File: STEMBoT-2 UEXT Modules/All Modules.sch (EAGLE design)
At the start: 132 parts, among them IC1 74HC165PW,118, IC2 74HC165PW,118, IC3 74HC165PW,118, J1 FTSH-105-01-XXX-DV-K, J2 FTSH-105-01-XXX-DV-K, J3 FTSH-105-01-XXX-DV-K, J4 FTSH-105-01-XXX-DV-K, J5 FTSH-105-01-XXX-DV-K, J6 FTSH-105-01-XXX-DV-K, Q1 MMBT3904LP-7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

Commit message: final pcb board layout for reveiw
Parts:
- added R56, R59, R60: ERJ-1RHD3601C, Resistor:ERJ-1RHD3601C
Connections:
- removed net N$145: IC2.!PL, U$2.MOSI
- removed net N$159: R61.1
- removed net N$163: IC3.!PL, U$1.MOSI
- removed net N$2: U1.OUT
- new net N$158: IC3.!PL, R56.1, U$1.MOSI
- new net N$164: IC2.!PL, R60.1, U$2.MOSI
- net N$100: now also U4.3; no longer U4.4
- net N$125: now also U1.OUT
- net N$157: now also R61.1
- net N$162: now also R59.1
- net N$20: no longer IC1.DS
- net N$39: now also IC1.D3, IC1.D4, IC1.D5, IC1.D6, IC1.D7, R59.2
- net N$43: now also U7.4; no longer U7.3
- net N$44: now also U7.3; no longer U7.4
- net N$53: no longer IC2.DS
- net N$55: now also R56.2
- net N$64: now also IC2.D3, IC2.D4, IC2.D5, IC2.D6, IC2.D7, R60.2
- net N$68: now also U10.4; no longer U10.3
- net N$69: now also U10.3; no longer U10.4
- net N$99: now also U4.4; no longer U4.3
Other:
- moved on the sheet: R30, R61

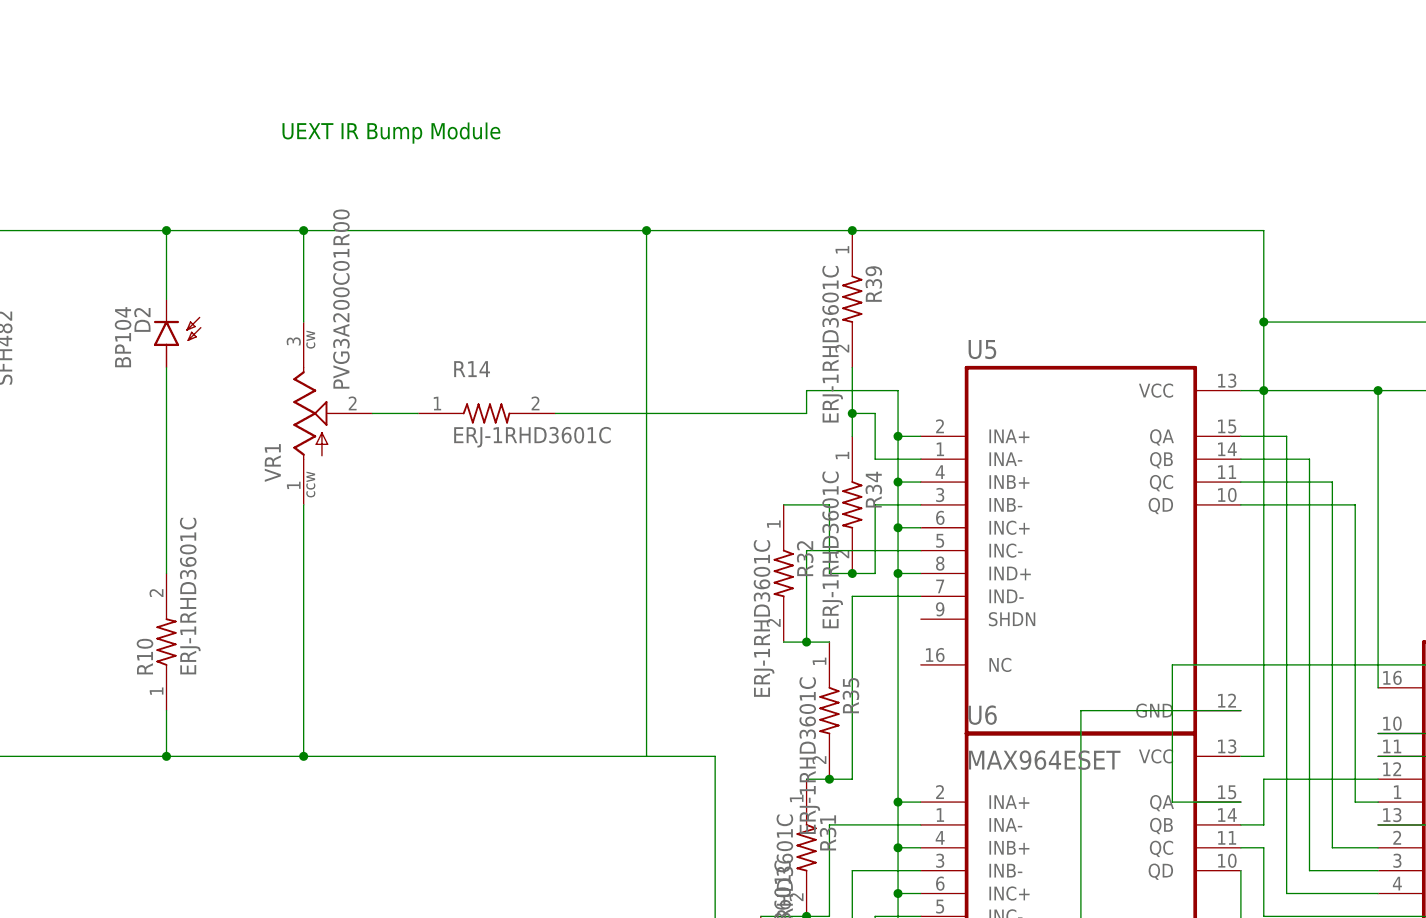
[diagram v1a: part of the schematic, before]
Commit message: I am a little wary off all this stuff in here. I went ahead and added an ultrasonic schem in here. Dont know why it wasnt in before.
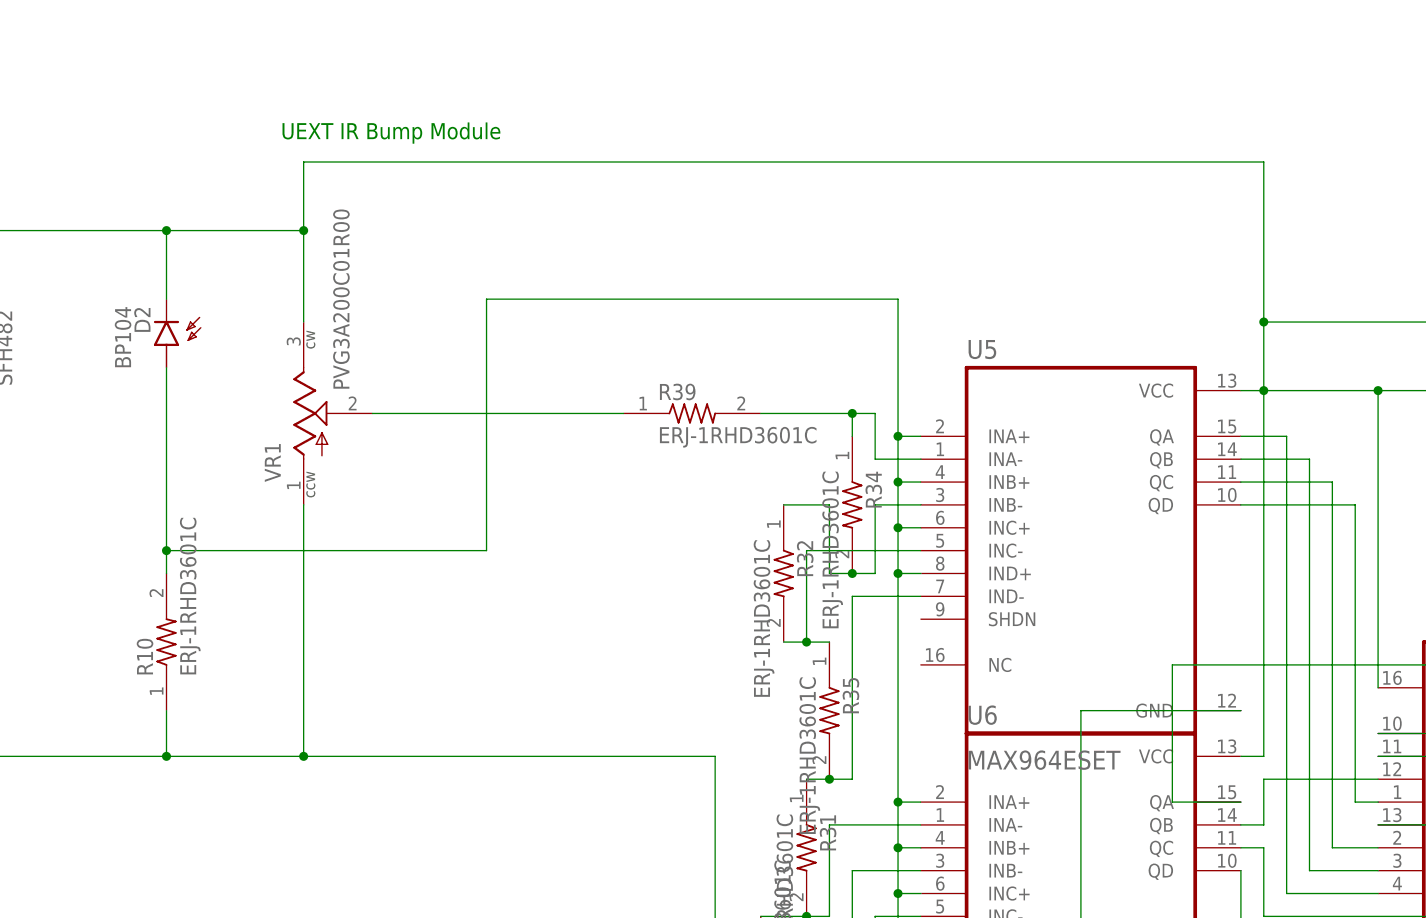
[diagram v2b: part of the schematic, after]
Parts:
- removed R14: ERJ-1RHD3601C, Resistor:ERJ-1RHD3601C
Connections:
- removed net N$70: D2.A, R10.2
- removed net N$79: R14.2, U5.INA+, U5.INB+, U5.INC+, U5.IND+, U6.INA+, U6.INB+, U6.INC+, U6.IND+
- new net N$145: R39.1, VR1.WIPER
- new net N$2: D1.A, D2.C, IC3.VCC, R11.1, R12.2, U$1.3.3V, U4.VCC, U5.VCC, U6.VCC, VR1.CW
- net N$55: no longer D1.A, D2.C, IC3.VCC, R11.1, R12.2, R39.1, U$1.3.3V, U4.VCC, U5.VCC, U6.VCC, VR1.CW
- net N$71: now also D2.A, R10.2, U5.INA+, U5.INB+, U5.INC+, U5.IND+, U6.INA+, U6.INB+, U6.INC+, U6.IND+; no longer R14.1, VR1.WIPER
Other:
- moved on the sheet: R39
